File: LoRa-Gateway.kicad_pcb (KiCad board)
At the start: 2 copper layers, 37 parts, among them IC1 LT8609MSE, J1 Conn_01x06, J2 Barrel_Jack, J3 Conn_Coaxial, U1 ESP-12E, U2 RFM95W-868S2

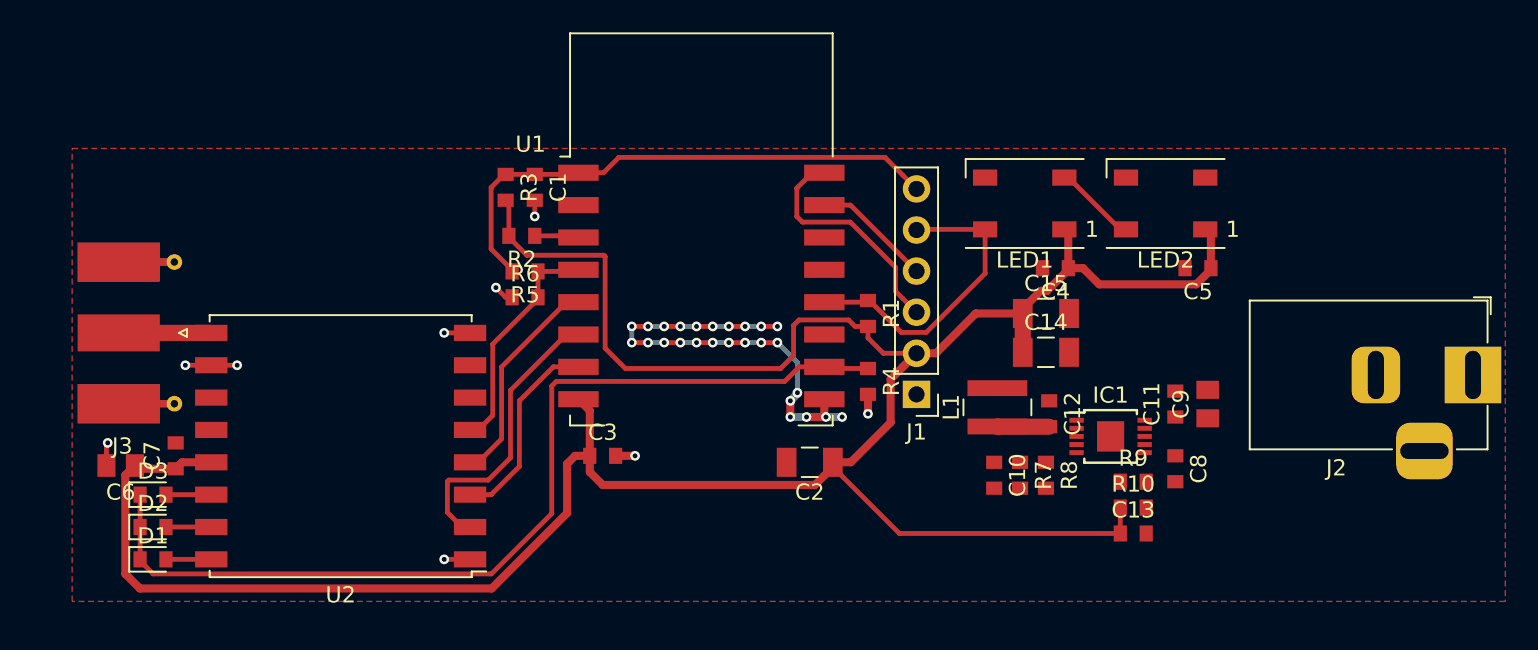
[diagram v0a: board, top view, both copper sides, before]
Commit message: Changed barrel plug to terminal block
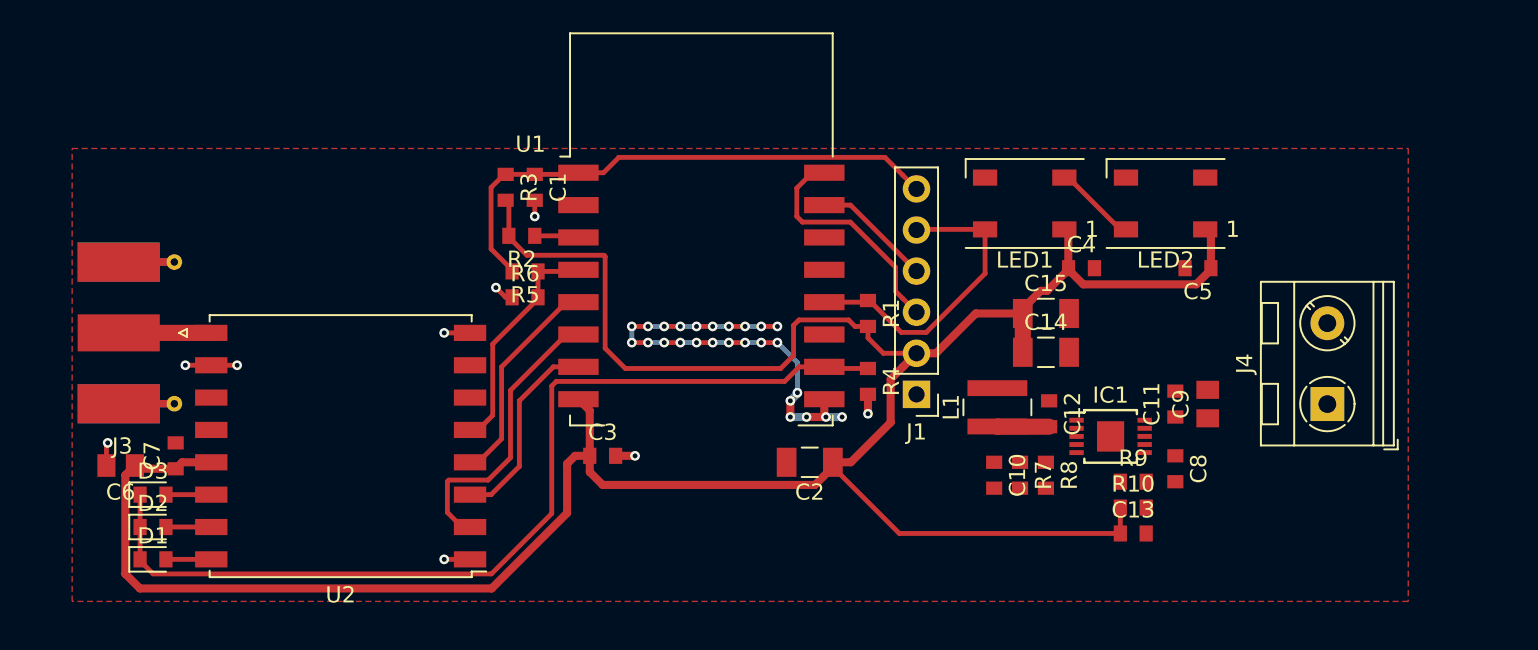
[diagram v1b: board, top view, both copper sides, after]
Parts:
- removed J2: Barrel_Jack, Connector_BarrelJack:BarrelJack_Horizontal
- added J4: Conn_01x02, TerminalBlock_RND:TerminalBlock_RND_205-00045_1x02_P5.00mm_Horizontal, F.Cu at (194.0, 72.8)
- moved C4 1.62 mm to (178.8, 64.4), turned to 0 degrees

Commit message: Routed DC-DC convertor, added vias under ESP8266 for better cooling
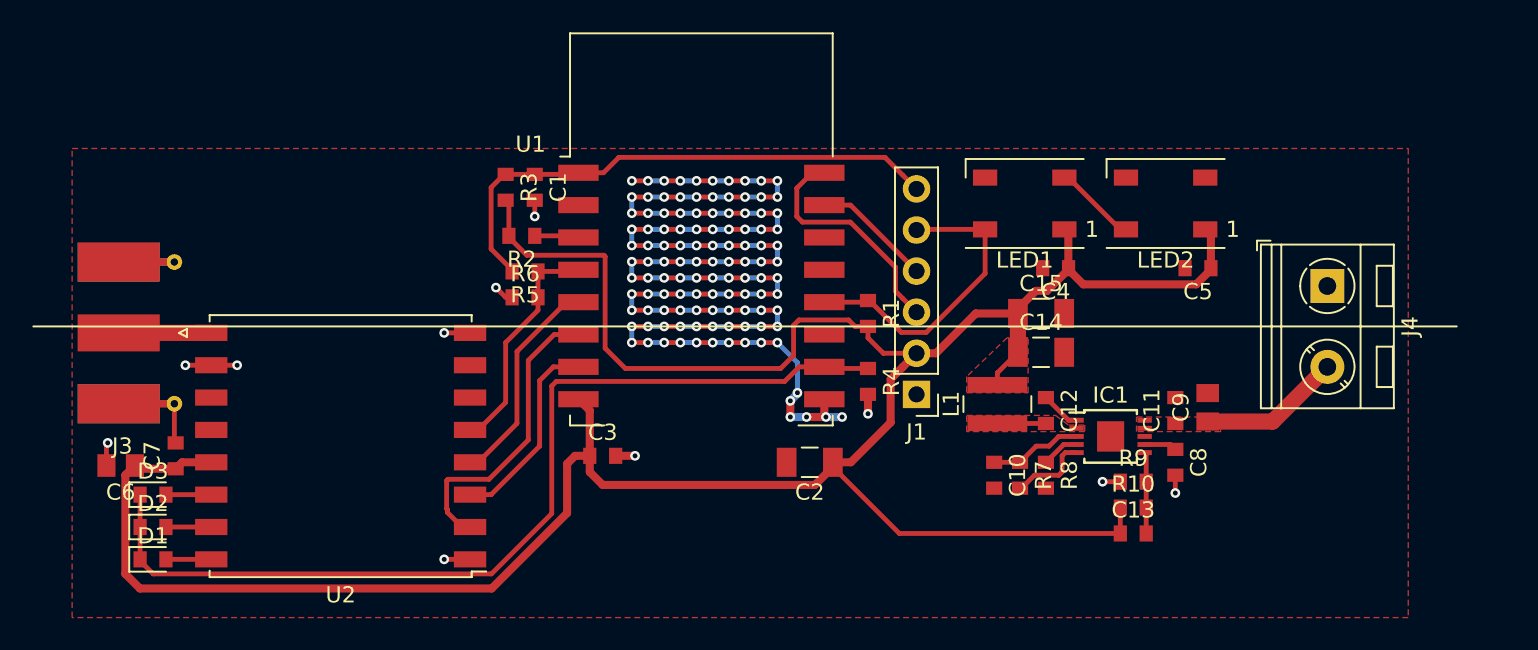
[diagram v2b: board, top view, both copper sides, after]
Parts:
- moved J4 7.30 mm to (194.0, 65.5), turned to 270 degrees
- moved C4 1.60 mm to (177.2, 64.4), turned to 180 degrees
- moved C11 0.40 mm to (184.6, 73.2)
- moved C8 0.40 mm to (184.6, 76.4)
- moved C14 0.30 mm to (176.3, 69.6)
- moved C15 0.30 mm to (176.3, 67.2)
- moved C12 0.28 mm to (176.6, 73.2)
- moved C9 0.20 mm to (186.6, 73.0)
- moved L1 0.20 mm to (173.6, 72.8)
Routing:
- net GND: track 41.1 -> 135.8 mm, vias 35 -> 127
- net VCC: track 0.00 -> 8.80 mm
- net Net-(C10-Pad1): track 0.00 -> 5.76 mm
- net Net-(C13-Pad2): track 0.00 -> 5.04 mm
- net Net-(IC1-Pad5): track 0.00 -> 4.99 mm
- net +3V3: track 164.5 -> 167.3 mm
- net Net-(C12-Pad1): track 0.00 -> 2.47 mm
- net Net-(IC1-Pad4): track 0.00 -> 2.35 mm
- net Net-(C8-Pad1): track 0.00 -> 2.02 mm
- net /MISO: track 18.0 -> 18.5 mm
- added copper zone on F.Cu, net +3V3
- added copper zone on F.Cu, net Net-(C12-Pad2)
- added copper zone on F.Cu, net VCC
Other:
- net class Default: clearance 0.25 -> 0.3
- rule trace_clearance: 0.25 -> 0.3

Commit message: Grounding improvement, dimmensions set
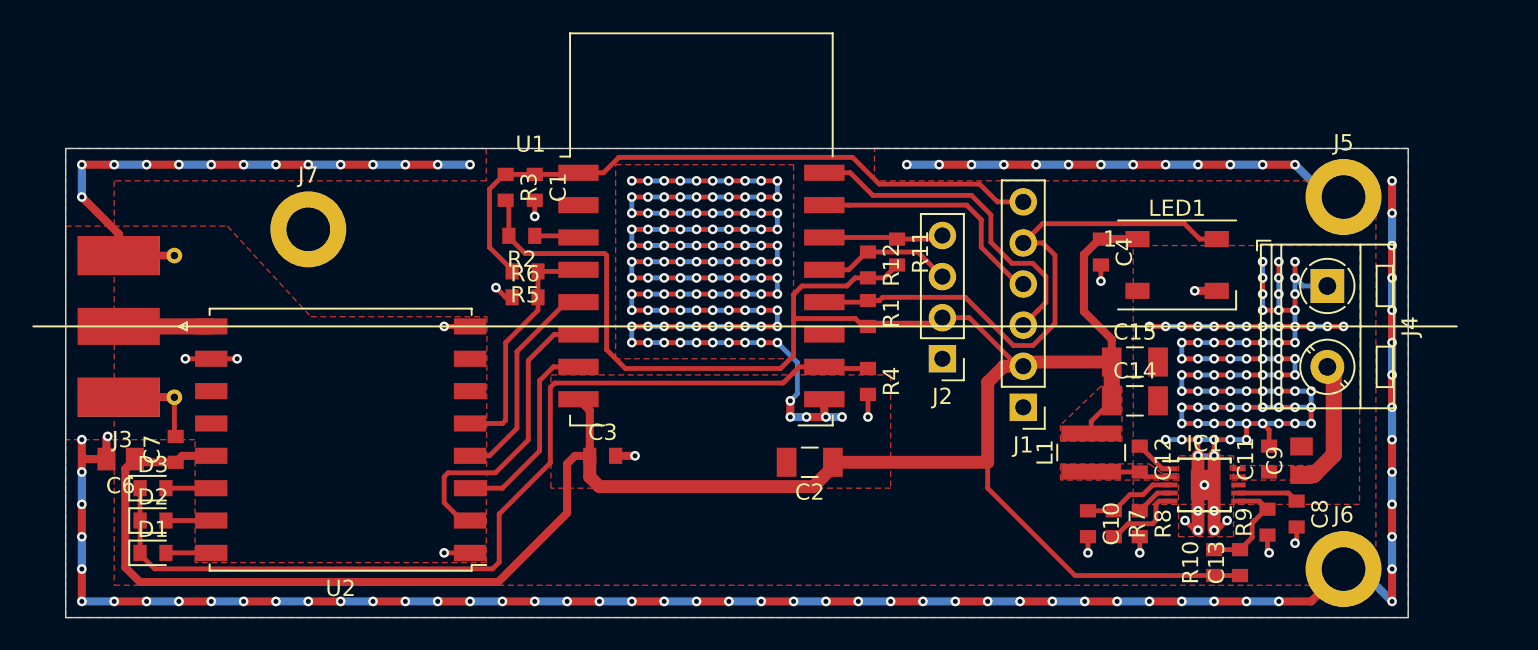
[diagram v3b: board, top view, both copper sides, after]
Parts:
- removed C5: 100n, Capacitor_SMD:C_0603_1608Metric
- removed LED2: WS2812B, LED_SMD:LED_WS2812B_PLCC4_5.0x5.0mm_P3.2mm
- added J2: Conn_01x04, Connector_PinHeader_2.54mm:PinHeader_1x04_P2.54mm_Vertical, F.Cu at (170.2, 70.0)
- added J5: Conn_01x01, MountingHole:MountingHole_2.7mm_M2.5_DIN965_Pad, F.Cu at (195.0, 60.0)
- added J6: Conn_01x01, MountingHole:MountingHole_2.7mm_M2.5_DIN965_Pad, F.Cu at (195.0, 83.0)
- added J7: Conn_01x01, MountingHole:MountingHole_2.7mm_M2.5_DIN965_Pad, F.Cu at (131.0, 62.0)
- added R11: DNP, Resistor_SMD:R_0603_1608Metric, F.Cu at (167.4, 63.4)
- added R12: DNP, Resistor_SMD:R_0603_1608Metric, F.Cu at (165.6, 64.2)
- C13: value 1u -> 10p
- R10: value 18k -> 220k
- R9: value 18k -> 68k
- moved LED1 10.2 mm to (184.7, 64.2), turned to 0 degrees
- moved R9 8.67 mm to (190.3, 80.1), turned to 90 degrees
- moved C8 8.15 mm to (192.1, 79.6)
- moved C13 6.84 mm to (188.6, 82.6), turned to 90 degrees
- moved C9 6.67 mm to (192.4, 76.3)
- moved J1 6.65 mm to (175.2, 73.0)
- moved C11 6.53 mm to (190.4, 76.2)
- moved C12 6.53 mm to (182.4, 76.2)
- moved IC1 6.53 mm to (186.4, 77.8)
- moved L1 6.53 mm to (179.4, 75.8)
- moved R7 6.53 mm to (180.8, 80.2)
- moved R8 6.53 mm to (182.4, 80.2)
- moved C10 6.53 mm to (179.2, 80.2)
- moved C14 6.53 mm to (182.1, 72.6)
- moved C15 6.53 mm to (182.1, 70.2)
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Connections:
- IC1 pad 11: (no net) -> GND
- U1 pad 19: (no net) -> /SDA
- U1 pad 20: (no net) -> /SCL
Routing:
- net GND: track 135.8 -> 421.2 mm, vias 127 -> 305
- net /GPIO0: track 19.3 -> 35.5 mm
- net +3V3: track 167.3 -> 179.6 mm
- net /SDA: track 0.00 -> 8.39 mm
- net /RX: track 7.39 -> 15.3 mm
- net /SCL: track 0.00 -> 7.43 mm
- net /RES: track 33.6 -> 40.6 mm
- net /TX: track 14.6 -> 20.9 mm
- net Net-(LED1-Pad2): track 5.14 -> 0.00 mm
- net Net-(C12-Pad2): track 3.01 -> 5.03 mm
- net Net-(C13-Pad2): track 5.04 -> 6.88 mm
- net Net-(C8-Pad1): track 2.02 -> 3.80 mm
- net VCC: track 8.80 -> 8.12 mm
- added copper zone on B.Cu, net GND
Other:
- board outline added: 83 x 29 mm
- net class Default: clearance 0.3 -> 0.25
- rule trace_clearance: 0.3 -> 0.25

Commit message: Silk screen finished
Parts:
- added C1: 47u, Capacitor_SMD:C_1206_3216Metric, F.Cu at (152.2, 77.6)
- moved C2 7.30 mm to (154.8, 77.6), turned to 90 degrees
- moved J6 2.24 mm to (130.0, 60.0)
- renumbered C12 to C10, C14 to C11, C15 to C12, C8 to C14, C10 to C15, C6 to C4, C7 to C5, C1 to C6, C4 to C7, C9 to C8, C11 to C9, J3 to J1, J1 to J2, J2 to J3, J6 to J5, J7 to J6, J5 to J7, R5 to R1, R9 to R11, R8 to R12, R6 to R2, R1 to R3, R2 to R4, R3 to R5, R4 to R6, R11 to R7, R12 to R8, R7 to R9, U2 to U1, U1 to U2
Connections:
- LED1 pad 2: Net-(LED1-Pad2) -> (no net)
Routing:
- net VCC: track 8.12 -> 12.6 mm
- net GND: track 421.2 -> 423.9 mm
- net +3V3: track 179.6 -> 181.8 mm
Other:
- board text added: "LoRa Gateway 190910"
- board text added: "RES G0 RX TX 3V3 GND"
- board text added: "SCL SDA 3V3 GND"

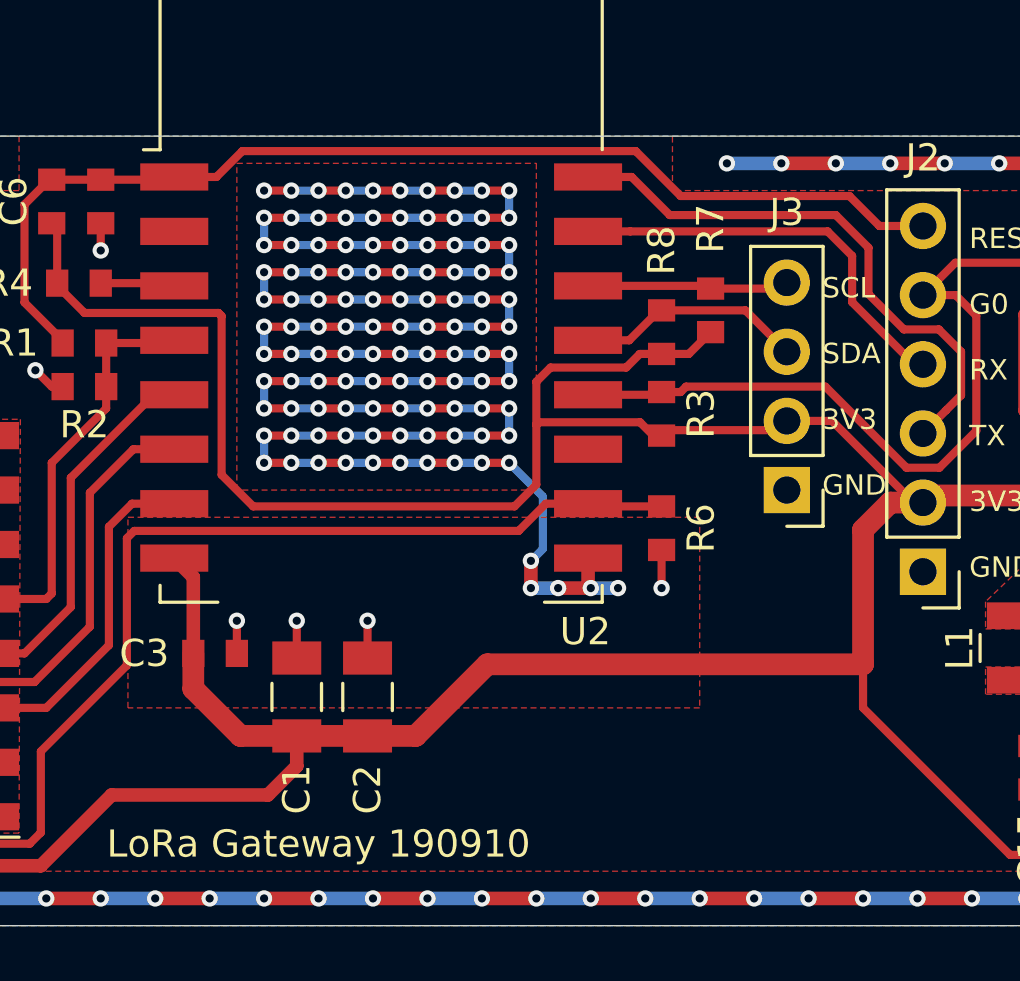
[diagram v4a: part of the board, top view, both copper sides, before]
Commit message: Edited mask under the ESP8266 for better cooling. Silkscreen improvement.
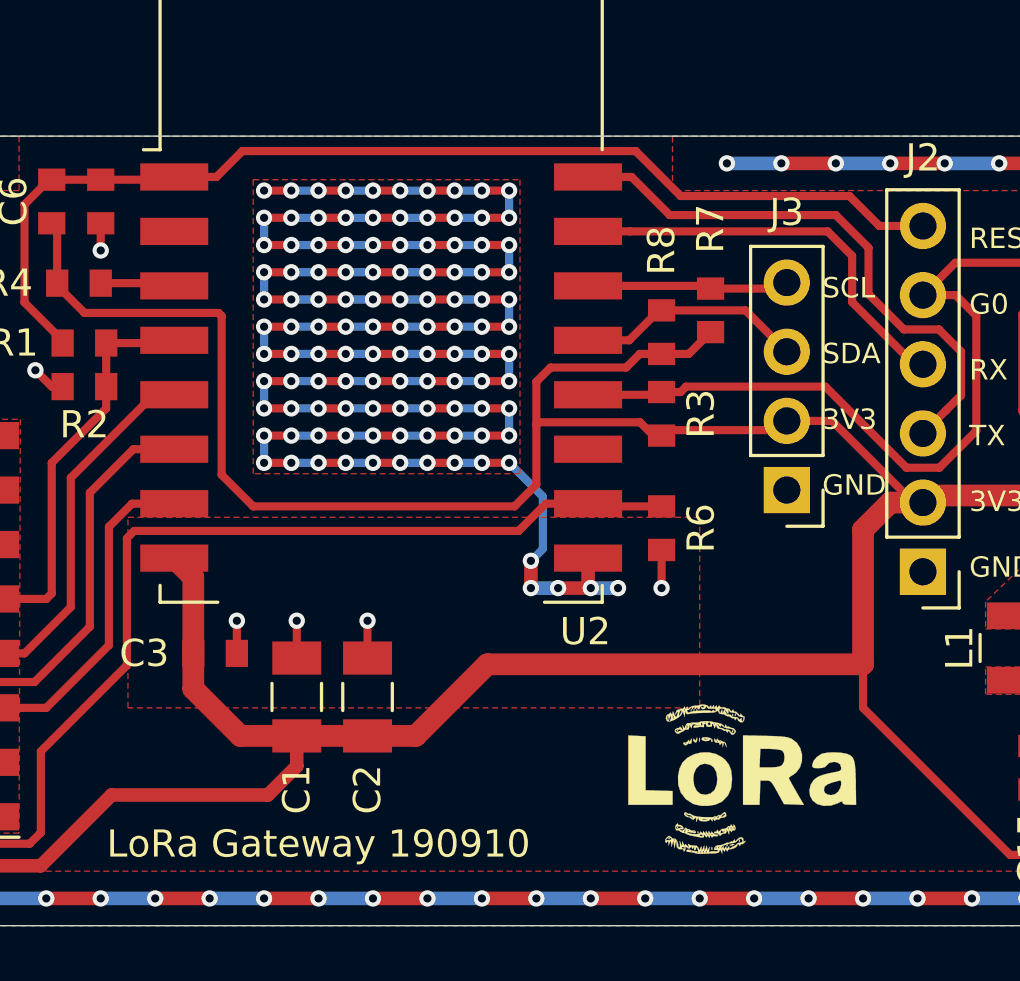
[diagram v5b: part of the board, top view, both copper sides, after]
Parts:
- added G***: RiskeLogo, kicad-footprints-master:RiskeLogo, B.Cu at (133.0, 71.0)
- added G***: LoRa-Logo-Small, kicad-footprints-master:LoRa-Logo-Small, F.Cu at (169.0, 81.0)
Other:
- board text added: "GND max. 40V"

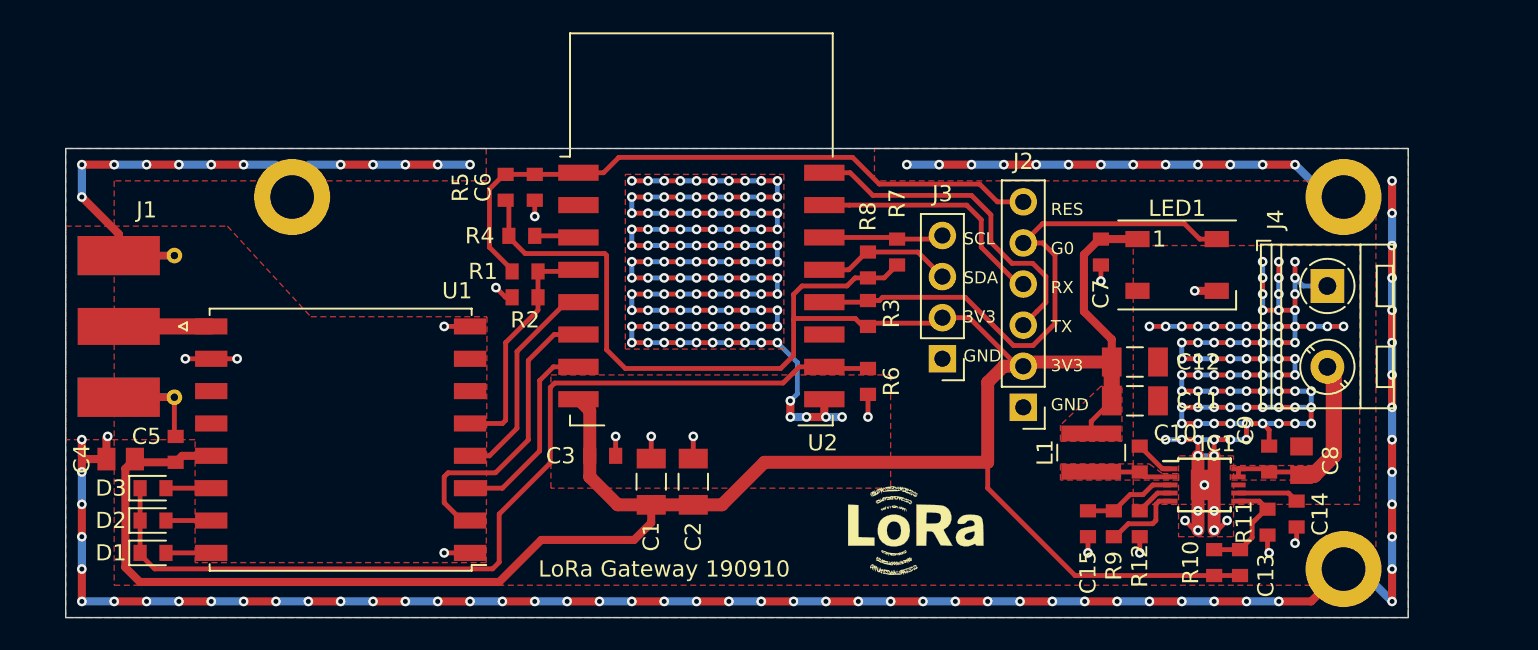
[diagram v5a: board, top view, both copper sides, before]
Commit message: Added protection diode, changed antenna connector
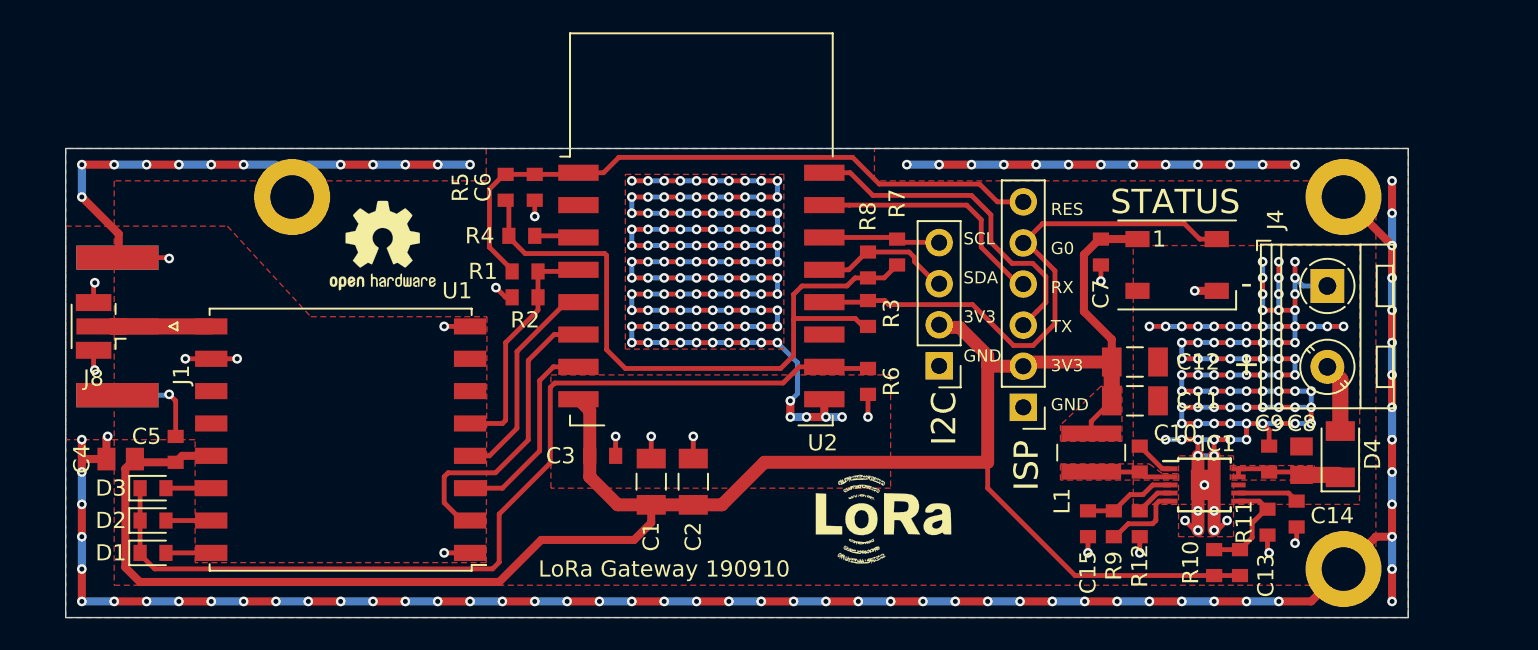
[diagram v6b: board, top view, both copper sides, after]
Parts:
- removed the G*** at (133.0, 71.0)
- removed the G*** at (169.0, 81.0)
- added D4: D, Diode_SMD:D_1206_3216Metric, F.Cu at (194.8, 75.9)
- added G***: RiskeLogo, MYLIB:RiskeLogo, B.Cu at (133.1, 70.6)
- added G***: LoRa-Logo-Small, MYLIB:LoRa-Logo-Small, F.Cu at (167.0, 80.3)
- added J8: Conn_Coaxial, Connector_Coaxial:U.FL_Hirose_U.FL-R-SMT-1_Vertical, F.Cu at (118.2, 68.0)
- added REF**: OSHW-Logo2_7.3x6mm_SilkScreen, Symbol:OSHW-Logo2_7.3x6mm_SilkScreen, F.Cu at (135.6, 63.0)
- J1: footprint Connector_Coaxial:SMA_Molex_73251-1153_EdgeMount_Horizontal -> Connector_Coaxial:SMA_Amphenol_132289_EdgeMount
- moved J1 1.80 mm to (119.2, 68.0), turned to 180 degrees
- moved J3 0.48 mm to (170.0, 70.4)
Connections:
- net Net-(J1-Pad1) renamed /ANT
- IC1 pad 8: (no net) -> Net-(IC1-Pad8)
- J4 pad 2: VCC -> Net-(D4-Pad2)
- LED1 pad 2: (no net) -> Net-(LED1-Pad2)
- U1 pad 11: (no net) -> Net-(U1-Pad11)
- U1 pad 12: (no net) -> Net-(U1-Pad12)
- U1 pad 6: (no net) -> Net-(U1-Pad6)
- U1 pad 7: (no net) -> Net-(U1-Pad7)
- U2 pad 17: (no net) -> Net-(U2-Pad17)
- U2 pad 2: (no net) -> Net-(U2-Pad2)
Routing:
- net GND: track 423.9 -> 435.6 mm, vias 305 -> 309
- net +3V3: track 181.8 -> 175.7 mm
- net VCC: track 12.6 -> 6.96 mm
- net Net-(D4-Pad2): track 0.00 -> 4.10 mm
- net /GPIO0: track 35.5 -> 34.8 mm
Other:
- board text added: "+ -"
- board text added: "I2C"
- board text added: "ISP"
- board text added: "STATUS"
